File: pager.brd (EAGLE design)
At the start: 78.4 x 44.8 mm, 65 parts, among them Q1 25 MHz, Q2 SI2333DS, SW1 CHS-01A1, SW2 CHS-01A1, U1 VOCORE2-SMD, U2 VOCORE2-SMD, U3 XR22800IL, U4 IP4234CZ6, X1 OMRON_XF2L-30REVERSE, X2 FCI_8193_MICRO_USB

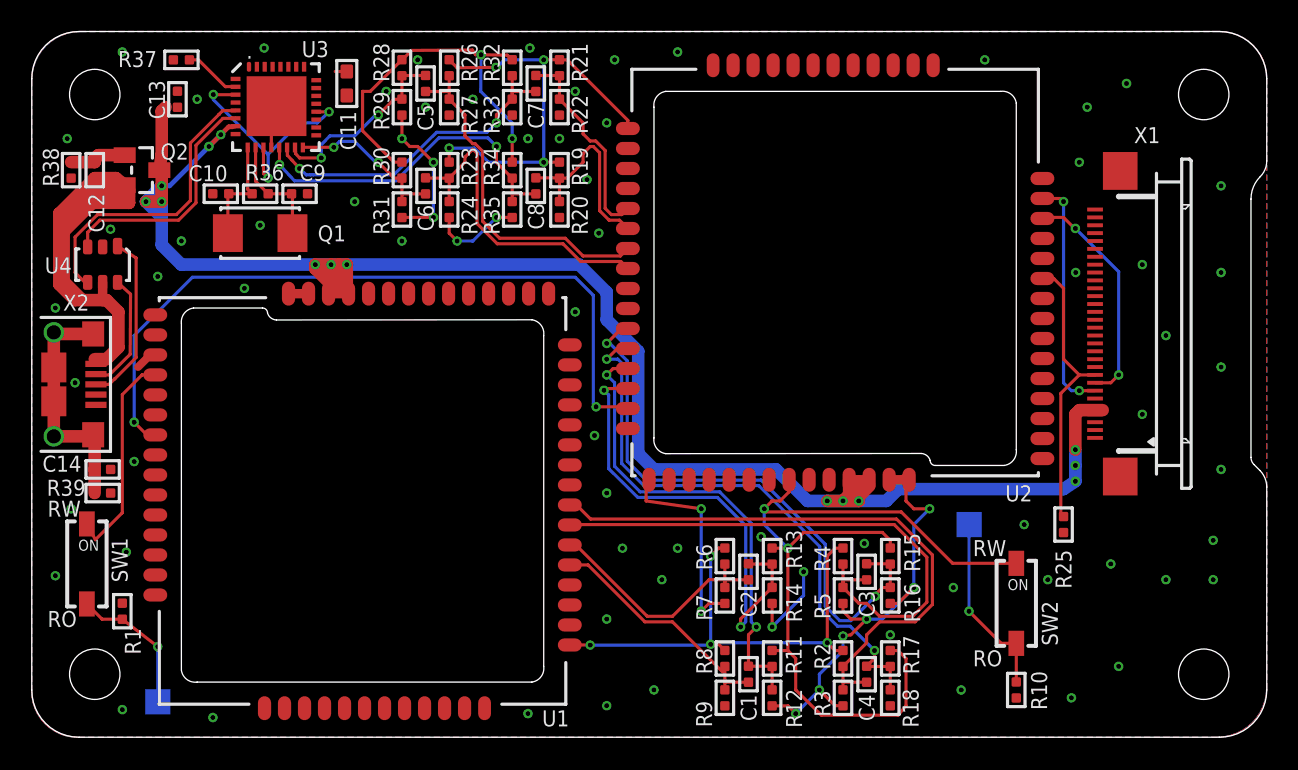
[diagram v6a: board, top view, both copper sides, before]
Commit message: Moved vias away from under metallic components
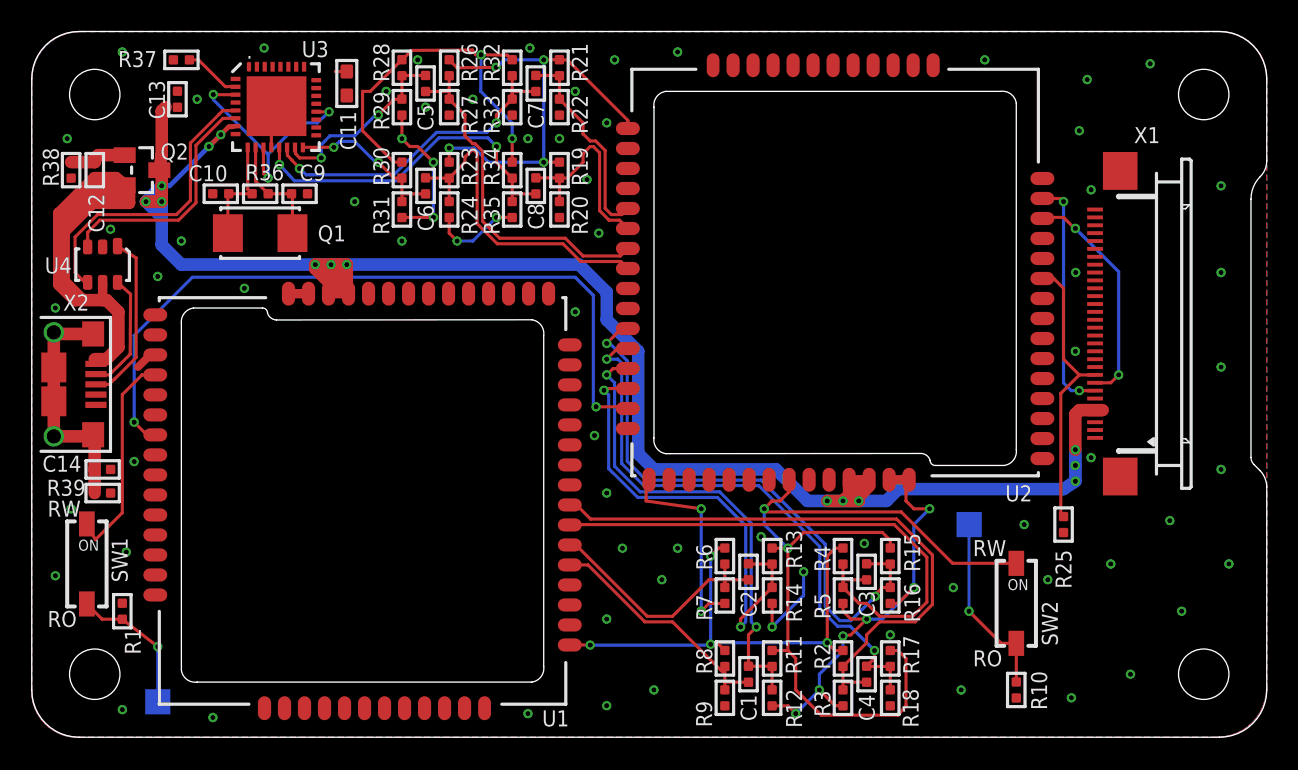
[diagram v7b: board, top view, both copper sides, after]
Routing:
- net GND: vias 82 -> 80
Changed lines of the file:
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@@
 <wire x1="51.5" y1="6.425" x2="52" y2="6.5" width="0.2" layer="1"/>
 <wire x1="52" y1="6.5" x2="53" y2="7.5" width="0.2" layer="1"/>
-<via x="67" y="40" extent="1-16" drill="0.3048"/>
+<via x="67" y="41.75" extent="1-16" drill="0.3048"/>
 <via x="41" y="12" extent="1-16" drill="0.3048"/>
-<via x="69" y="4.5" extent="1-16" drill="0.3048"/>
-<via x="69.5" y="41.5" extent="1-16" drill="0.3048"/>
+<via x="69.75" y="4" extent="1-16" drill="0.3048"/>
+<via x="71" y="42.75" extent="1-16" drill="0.3048"/>
 <via x="39.5" y="3" extent="1-16" drill="0.3048"/>
 <via x="36.5" y="2" extent="1-16" drill="0.3048"/>
@@
 <via x="60.5" y="43" extent="1-16" drill="0.3048"/>
 <via x="75.5" y="35" extent="1-16" drill="0.3048"/>
-<via x="70.5" y="30" extent="1-16" drill="0.3048"/>
+<wire x1="70.5" y1="30" x2="70.5" y2="30" width="0" layer="19" extent="1-16"/>
 <via x="75.5" y="23.5" extent="1-16" drill="0.3048"/>
-<via x="70.5" y="20.5" extent="1-16" drill="0.3048"/>
-<via x="75" y="10" extent="1-16" drill="0.3048"/>
+<wire x1="70.5" y1="20.5" x2="70.5" y2="20.5" width="0" layer="19" extent="1-16"/>
+<via x="73" y="8" extent="1-16" drill="0.3048"/>
 <via x="68.5" y="11" extent="1-16" drill="0.3048"/>
 <via x="63" y="13.5" extent="1-16" drill="0.3048"/>
@@
 <wire x1="15.21" y1="37.44" x2="15.21" y2="39.73" width="0.2" layer="1"/>
 <wire x1="15.21" y1="39.73" x2="15.54" y2="40.06" width="0.2" layer="1"/>
-<via x="75" y="12.5" extent="1-16" drill="0.3048"/>
+<via x="76" y="11" extent="1-16" drill="0.3048"/>
 <via x="75.5" y="17" extent="1-16" drill="0.3048"/>
 <via x="75.5" y="29.5" extent="1-16" drill="0.3048"/>
@@
 <via x="35.25" y="35.4" extent="1-16" drill="0.3048"/>
 <via x="9.5" y="31.5" extent="1-16" drill="0.3048"/>
-<via x="14.5" y="32.5" extent="1-16" drill="0.3048"/>
-<via x="72" y="10" extent="1-16" drill="0.3048"/>
-<via x="66.5" y="36.5" extent="1-16" drill="0.3048"/>
-<via x="72" y="25.5" extent="1-16" drill="0.3048"/>
+<wire x1="14.5" y1="32.5" x2="14.5" y2="32.5" width="0" layer="19" extent="1-16"/>
+<via x="72.25" y="13.75" extent="1-16" drill="0.3048"/>
+<via x="66.5" y="38.5" extent="1-16" drill="0.3048"/>
+<wire x1="72" y1="25.5" x2="72" y2="25.5" width="0" layer="19" extent="1-16"/>
 <via x="66.275" y="29.5" extent="1-16" drill="0.3048"/>
 <via x="23.5" y="38" extent="1-16" drill="0.3048"/>
@@
 <via x="10.5" y="40.5" extent="1-16" drill="0.3048"/>
 <wire x1="7.5" y1="24.25" x2="6.75" y2="23.5" width="0.5" layer="1"/>
-<via x="2.75" y="22.5" extent="1-16" drill="0.3048"/>
+<wire x1="2.75" y1="22.5" x2="2.75" y2="22.5" width="0" layer="19" extent="1-16"/>
 <via x="14.75" y="43.75" extent="1-16" drill="0.3048"/>
 <via x="5" y="32.25" extent="1-16" drill="0.3048"/>
@@
 <wire x1="49" y1="9" x2="49" y2="10.5" width="0.2" layer="16"/>
 <via x="1.5" y="27.25" extent="1-16" drill="0.3048"/>
+<via x="67.25" y="17.75" extent="1-16" drill="0.3048"/>
+<via x="67.25" y="34.75" extent="1-16" drill="0.3048"/>
+<via x="66.25" y="24.5" extent="1-16" drill="0.3048"/>
 </signal>
 <signal name="ETH_1B_TX_P" class="1">

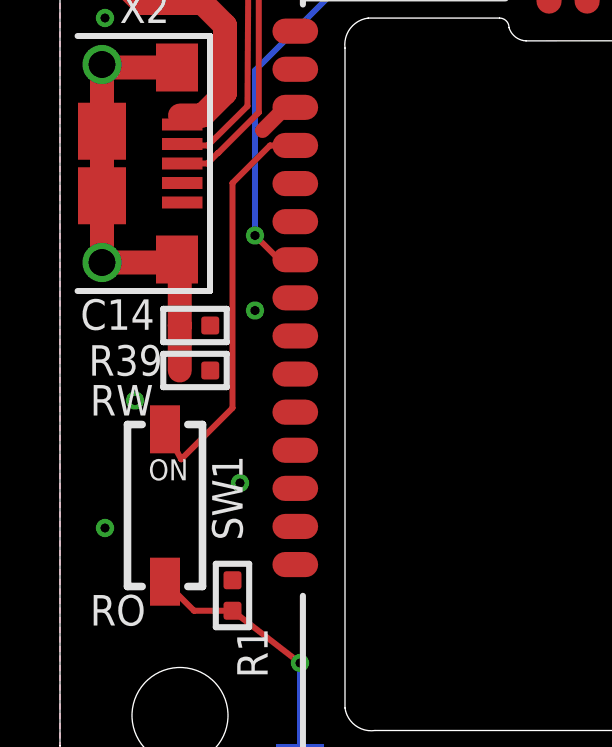
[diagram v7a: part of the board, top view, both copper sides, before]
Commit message: fix to a trace
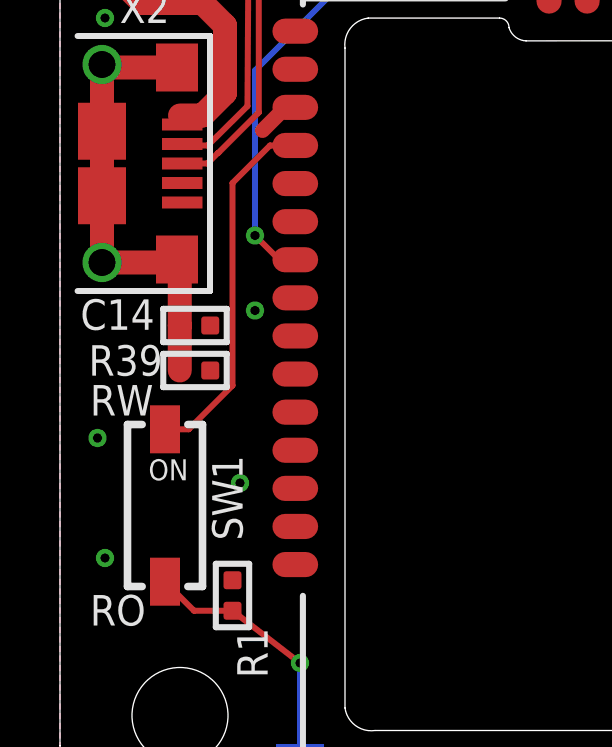
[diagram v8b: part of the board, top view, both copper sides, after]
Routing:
- net 3.3_WIFI: track 45.8 -> 44.3 mm
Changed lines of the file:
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@@
 <via x="60.5" y="43" extent="1-16" drill="0.3048"/>
 <via x="75.5" y="35" extent="1-16" drill="0.3048"/>
-<wire x1="70.5" y1="30" x2="70.5" y2="30" width="0" layer="19" extent="1-16"/>
 <via x="75.5" y="23.5" extent="1-16" drill="0.3048"/>
-<wire x1="70.5" y1="20.5" x2="70.5" y2="20.5" width="0" layer="19" extent="1-16"/>
 <via x="73" y="8" extent="1-16" drill="0.3048"/>
 <via x="68.5" y="11" extent="1-16" drill="0.3048"/>
@@
 <via x="35.25" y="35.4" extent="1-16" drill="0.3048"/>
 <via x="9.5" y="31.5" extent="1-16" drill="0.3048"/>
-<wire x1="14.5" y1="32.5" x2="14.5" y2="32.5" width="0" layer="19" extent="1-16"/>
 <via x="72.25" y="13.75" extent="1-16" drill="0.3048"/>
 <via x="66.5" y="38.5" extent="1-16" drill="0.3048"/>
-<wire x1="72" y1="25.5" x2="72" y2="25.5" width="0" layer="19" extent="1-16"/>
 <via x="66.275" y="29.5" extent="1-16" drill="0.3048"/>
 <via x="23.5" y="38" extent="1-16" drill="0.3048"/>
@@
 <contactref element="C14" pad="2"/>
 <contactref element="R39" pad="1"/>
-<via x="2.5" y="14.5" extent="1-16" drill="0.3048"/>
-<via x="1.5" y="10.25" extent="1-16" drill="0.3048"/>
+<via x="1.25" y="13.25" extent="1-16" drill="0.3048"/>
+<via x="1.5" y="9.25" extent="1-16" drill="0.3048"/>
 <via x="5.75" y="1.75" extent="1-16" drill="0.3048"/>
 <via x="11.5" y="1.25" extent="1-16" drill="0.3048"/>
@@
 <via x="10.5" y="40.5" extent="1-16" drill="0.3048"/>
 <wire x1="7.5" y1="24.25" x2="6.75" y2="23.5" width="0.5" layer="1"/>
-<wire x1="2.75" y1="22.5" x2="2.75" y2="22.5" width="0" layer="19" extent="1-16"/>
 <via x="14.75" y="43.75" extent="1-16" drill="0.3048"/>
 <via x="5" y="32.25" extent="1-16" drill="0.3048"/>
@@
 <wire x1="7.8418" y1="23" x2="7" y2="23" width="0.2" layer="1"/>
 <wire x1="7" y1="23" x2="5.75" y2="21.75" width="0.2" layer="1"/>
-<wire x1="5.75" y1="21.75" x2="5.75" y2="14.25" width="0.2" layer="1"/>
-<wire x1="5.75" y1="14.25" x2="4.04" y2="12.54" width="0.2" layer="1"/>
-<wire x1="4.04" y1="12.54" x2="3.5" y2="13.54" width="0.2" layer="1"/>
+<wire x1="5.75" y1="21.75" x2="5.75" y2="15" width="0.2" layer="1"/>
+<wire x1="5.75" y1="15" x2="4.29" y2="13.54" width="0.2" layer="1"/>
+<wire x1="4.29" y1="13.54" x2="3.5" y2="13.54" width="0.2" layer="1"/>
 </signal>
 <signal name="WP_WIFI">
